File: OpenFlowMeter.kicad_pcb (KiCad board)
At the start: 2 copper layers, 70 x 28 mm, 72 parts, among them J1 Screw_Terminal_01x02, J2 Screw_Terminal_01x02, J3 Conn_01x06, J4 Conn_02x03_Odd_Even, J5 Conn_01x03, Q1 BC856, Q2 BC856, U1 LT1492, U2 STM32F103C8Tx, U3 LT1492, U4 R-78C3.3-1.0, U5 SN65HVD231, U6 LT1492, Y1 12 MHz

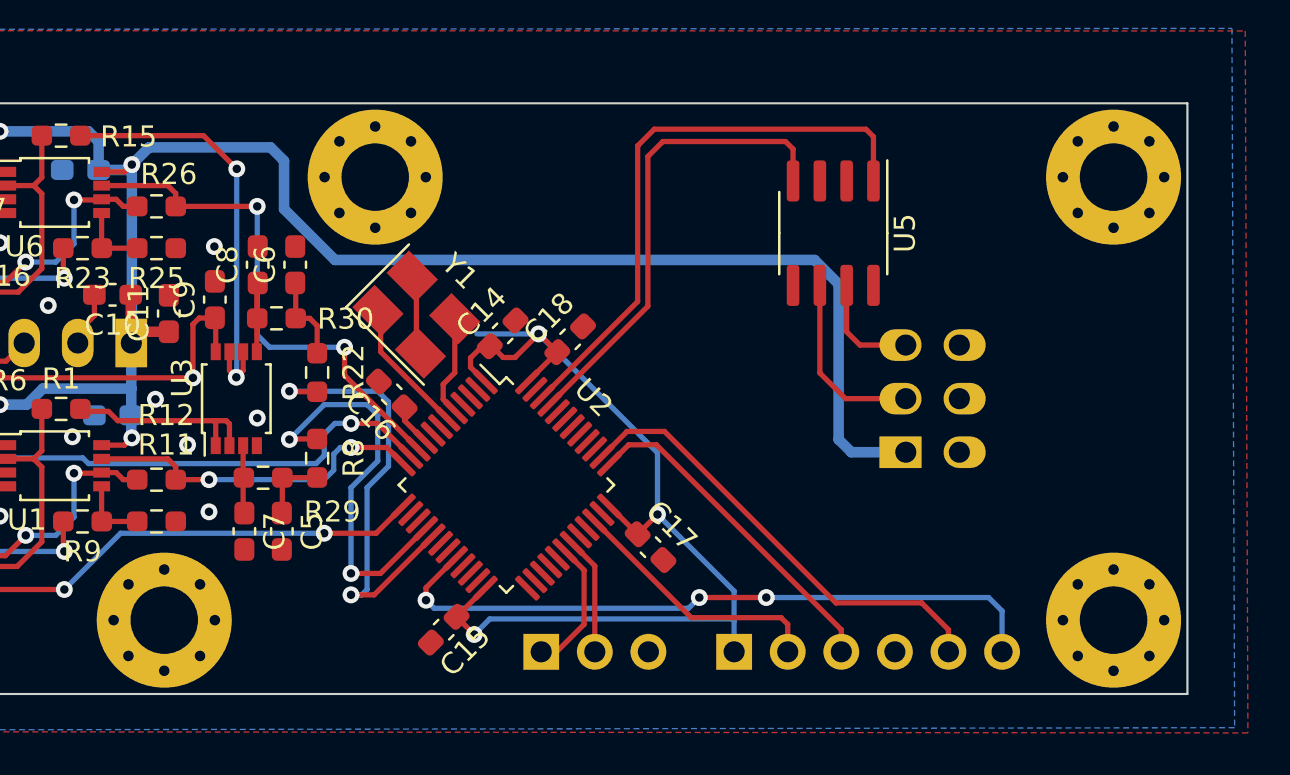
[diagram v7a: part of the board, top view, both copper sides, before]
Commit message: added LEDs and further routing
Added 4 LEDs, which can display the status
partially done routing of LEDs
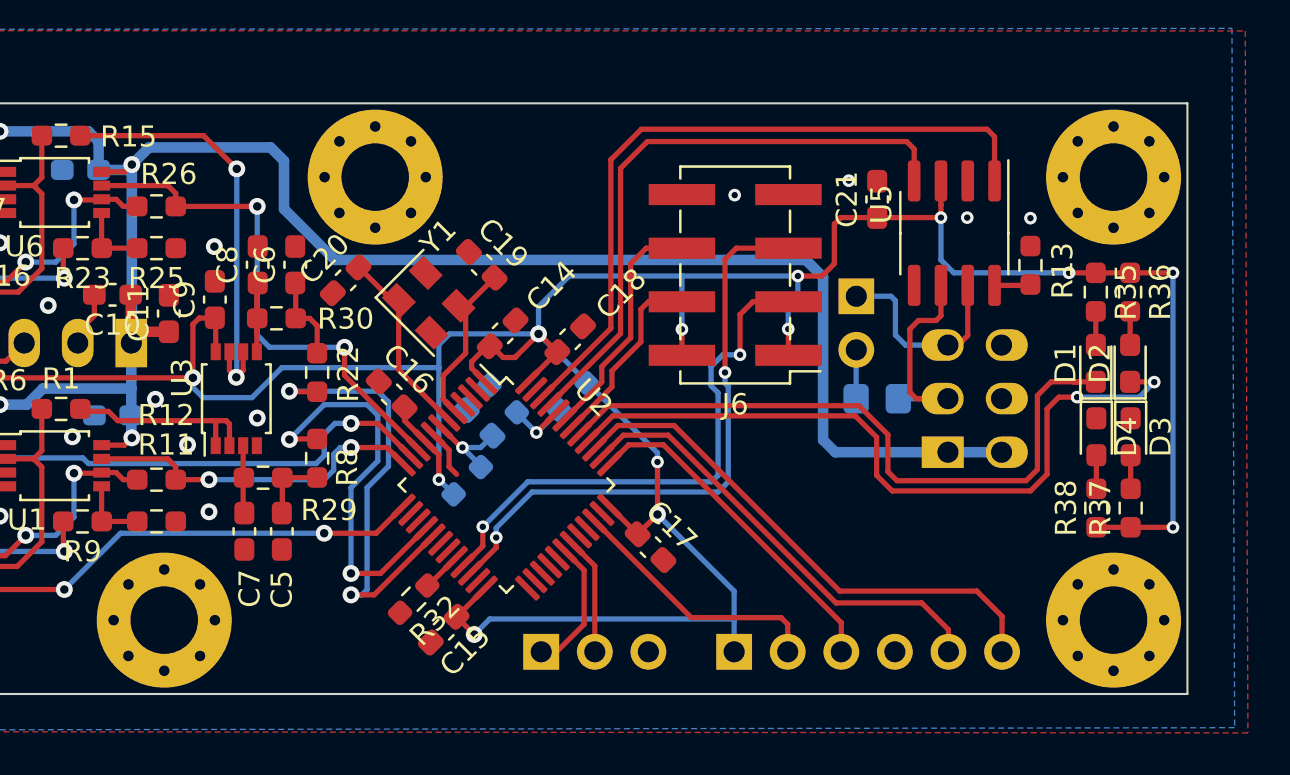
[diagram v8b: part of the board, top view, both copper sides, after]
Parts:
- added C19: C, Capacitor_SMD:C_0603_1608Metric_Pad1.08x0.95mm_HandSolder, F.Cu at (139.7, -17.6)
- added C20: C, Capacitor_SMD:C_0603_1608Metric_Pad1.08x0.95mm_HandSolder, F.Cu at (133.3, -16.8)
- added C21: 100n, Capacitor_SMD:C_0603_1608Metric_Pad1.08x0.95mm_HandSolder, F.Cu at (158.5, -20.7)
- added C22: 100n, Capacitor_SMD:C_0603_1608Metric_Pad1.08x0.95mm_HandSolder, B.Cu at (139.6, -10.1)
- added D1: LED, LED_SMD:LED_0603_1608Metric_Pad1.05x0.95mm_HandSolder, F.Cu at (168.8, -12.9)
- added D2: LED, LED_SMD:LED_0603_1608Metric_Pad1.05x0.95mm_HandSolder, F.Cu at (170.5, -12.9)
- added D3: LED, LED_SMD:LED_0603_1608Metric_Pad1.05x0.95mm_HandSolder, F.Cu at (170.5, -9.40)
- added D4: LED, LED_SMD:LED_0603_1608Metric_Pad1.05x0.95mm_HandSolder, F.Cu at (168.9, -9.40)
- added J6: Conn_02x04_Odd_Even, Connector_PinHeader_2.54mm:PinHeader_2x04_P2.54mm_Vertical_SMD, F.Cu at (151.7, -17.1)
- added JP1: Jumper_2_Open, Connector_PinHeader_2.54mm:PinHeader_1x02_P2.54mm_Vertical, B.Cu at (157.5, -16.1)
- added R13: 0, Resistor_SMD:R_0603_1608Metric_Pad0.98x0.95mm_HandSolder, F.Cu at (165.7, -17.5)
- added R14: 120, Resistor_SMD:R_0805_2012Metric_Pad1.20x1.40mm_HandSolder, B.Cu at (158.5, -11.2)
- added R31: 0, Resistor_SMD:R_0603_1608Metric_Pad0.98x0.95mm_HandSolder, B.Cu at (140.7, -11.2)
- added R32: 10k, Resistor_SMD:R_0603_1608Metric_Pad0.98x0.95mm_HandSolder, F.Cu at (136.5, -1.70)
- added R33: dnp, Resistor_SMD:R_0603_1608Metric_Pad0.98x0.95mm_HandSolder, B.Cu at (144.0, -11.3)
- added R34: 10k, Resistor_SMD:R_0603_1608Metric_Pad0.98x0.95mm_HandSolder, B.Cu at (139.0, -7.32)
- added R35: 10k, Resistor_SMD:R_0603_1608Metric_Pad0.98x0.95mm_HandSolder, F.Cu at (168.8, -16.3)
- added R36: 10k, Resistor_SMD:R_0603_1608Metric_Pad0.98x0.95mm_HandSolder, F.Cu at (170.5, -16.3)
- added R37: 10k, Resistor_SMD:R_0603_1608Metric_Pad0.98x0.95mm_HandSolder, F.Cu at (170.5, -6.02)
- added R38: 10k, Resistor_SMD:R_0603_1608Metric_Pad0.98x0.95mm_HandSolder, F.Cu at (168.9, -6.02)
- Y1: footprint Crystal:Crystal_SMD_EuroQuartz_MT-4Pin_3.2x2.5mm_HandSoldering -> Crystal:Crystal_SMD_EuroQuartz_MT-4Pin_3.2x2.5mm
- moved U5 5.74 mm to (162.1, -19.1)
- moved J4 2.00 mm to (168.2, -11.2)
- moved Y1 0.81 mm to (137.2, -15.7)
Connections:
- J4 pad 2: unconnected-(J4-Pad2) -> +24V
- J4 pad 4: unconnected-(J4-Pad4) -> GND
- U2 pad 20: /Controller/TDO -> Net-(R32-Pad1)
- U2 pad 39: unconnected-(U2-Pad39) -> /Controller/TDO
- U2 pad 40: unconnected-(U2-Pad40) -> /Controller/LED2
- U2 pad 41: unconnected-(U2-Pad41) -> /Controller/LED1
- U2 pad 44: unconnected-(U2-Pad44) -> Net-(U2-Pad44)
- U2 pad 7: unconnected-(U2-Pad7) -> Net-(U2-Pad7)
- U5 pad 3: unconnected-(U5-Pad3) -> +3V3
- U5 pad 8: unconnected-(U5-Pad8) -> Net-(U5-Pad8)
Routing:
- net +3V3: track 71.1 -> 157.1 mm, vias 4 -> 13
- net /Controller/LED2: track 0.00 -> 35.0 mm, vias 0 -> 2
- net /Controller/LED1: track 0.00 -> 31.7 mm
- net /Controller/I2C2_SDA: track 0.00 -> 28.4 mm, vias 0 -> 2
- net /Controller/I2C2_SCL: track 0.00 -> 25.8 mm, vias 0 -> 2
- net /Controller/I2C1_SDA: track 0.00 -> 11.4 mm
- net /Controller/I2C1_SCL: track 0.00 -> 9.01 mm
- net /Controller/TDO: track 33.2 -> 25.9 mm, vias 3 -> 0
- net /Controller/CAN_RX: track 22.5 -> 28.7 mm
- net /Controller/CAN_TX: track 27.5 -> 33.6 mm
- net +24V: track 91.1 -> 95.8 mm
- net /CAN H: track 5.26 -> 9.76 mm
- net Net-(U2-Pad7): track 0.00 -> 4.42 mm, vias 0 -> 1
- net Net-(U2-Pad44): track 0.00 -> 4.26 mm, vias 0 -> 1
- net /Controller/RCC_OSC_OUT: track 6.09 -> 8.96 mm
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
